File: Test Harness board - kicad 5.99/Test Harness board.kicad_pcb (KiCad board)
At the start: 4 copper layers, 233 x 70 mm, 133 parts, among them U1 TCA9548APWR

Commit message: restart with the test harness board
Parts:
- removed D_TEST1, D_TEST2: LED_Small, LED_SMD:LED_1206_3216Metric_Castellated
- UL1, UL3, UL4, UL5: footprint Package_SO:SSOP-28_5.3x10.2mm_P0.65mm -> Package_SO:TSSOP-28_4.4x9.7mm_P0.65mm
- UL1_1, UL1_2, UL2_1, UL2_2, UL3_1, UL3_2, UL4_1, UL4_2, UL5_1, UL5_2: footprint Package_SO:TSSOP-20_4.4x6.5mm_P0.65mm -> Package_SO:SOIC-20W_7.5x12.8mm_P1.27mm
- UL2: footprint Package_SO:SSOP-28_5.3x10.2mm_P0.65mm -> Package_SO:SOIC-28W_7.5x17.9mm_P1.27mm
- moved CL1_1 359.1 mm to (-151.7, 118.8), turned to 0 degrees
- moved CL3_2 334.8 mm to (-134.6, 102.0)
- moved CL4 325.0 mm to (-128.6, 95.4)
- moved UL3_1 316.4 mm to (-200.8, 111.7)
- moved D_A11 314.1 mm to (-217.1, 125.7), turned to 0 degrees
- moved CL4_1 310.9 mm to (-108.4, 76.0)
- moved CL1_2 310.9 mm to (-123.1, 90.7), turned to 0 degrees
- moved RNL3_1_2 307.7 mm to (-186.1, 109.6), turned to 0 degrees
- moved RNL1_1_2 305.8 mm to (-186.1, 102.8), turned to 0 degrees
- moved RNL1_2_2 298.9 mm to (-199.0, 122.3), turned to 0 degrees
- moved CL1 297.6 mm to (-96.3, 66.1)
- moved RNL3_2_2 291.3 mm to (-191.6, 102.8), turned to 0 degrees
- moved CL3 291.2 mm to (-95.5, 61.8)
- moved CL3_1 291.2 mm to (-84.0, 51.8)
- moved D_L11 289.8 mm to (-175.7, 124.5), turned to 0 degrees
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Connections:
- J_LEFT1 pad a11: Net-(J_LEFT1-Pada11) -> GND
- J_LEFT1 pad a15: Net-(J_LEFT1-Pada15) -> GND
- J_LEFT1 pad a17: Net-(J_LEFT1-Pada17) -> GND
- J_LEFT1 pad a19: Net-(J_LEFT1-Pada19) -> GND
- J_LEFT1 pad a32: Net-(J_LEFT1-Pada32) -> +5V
- J_LEFT1 pad a9: Net-(J_LEFT1-Pada9) -> GND
- J_LEFT1 pad b1: Net-(J_LEFT1-Padb1) -> +5V
- J_LEFT1 pad b11: Net-(J_LEFT1-Padb11) -> +5V
- J_LEFT1 pad b12: Net-(J_LEFT1-Padb12) -> GND
- J_LEFT1 pad b13: Net-(J_LEFT1-Padb13) -> +5V
- J_LEFT1 pad b17: Net-(J_LEFT1-Padb17) -> +5V
- J_LEFT1 pad b20: Net-(J_LEFT1-Padb20) -> GND
- J_LEFT1 pad b21: Net-(J_LEFT1-Padb21) -> +5V
- J_LEFT1 pad b22: Net-(J_LEFT1-Padb22) -> GND
- J_LEFT1 pad b23: Net-(J_LEFT1-Padb23) -> GND
- J_LEFT1 pad b24: Net-(J_LEFT1-Padb24) -> +5V
- J_LEFT1 pad b27: Net-(J_LEFT1-Padb27) -> +5V
- J_LEFT1 pad b31: Net-(J_LEFT1-Padb31) -> GND
- J_LEFT1 pad b32: Net-(J_LEFT1-Padb32) -> +5V
- J_LEFT1 pad c32: Net-(J_LEFT1-Padc32) -> +5V
- J_LEFT1 pad c9: Net-(J_LEFT1-Padc9) -> GND
- UL3 pad 1: /Left connector/A21 -> /Left connector/A13
- UL3 pad 2: /Left connector/A20 -> /Left connector/A12
- UL3 pad 21: /Left connector/A13 -> /Left connector/A21
- UL3 pad 22: /Left connector/A12 -> /Left connector/A20
- UL3 pad 23: /Left connector/A11 -> /Left connector/A19
- UL3 pad 24: /Left connector/A10 -> /Left connector/A18
- UL3 pad 25: /Left connector/A9 -> /Left connector/A17
- UL3 pad 26: /Left connector/A8 -> /Left connector/A16
- UL3 pad 27: /Left connector/A7 -> /Left connector/A15
- UL3 pad 28: /Left connector/A6 -> /Left connector/A14
- UL3 pad 3: /Left connector/A19 -> /Left connector/A11
- UL3 pad 4: /Left connector/A18 -> /Left connector/A10
- UL3 pad 5: /Left connector/A17 -> /Left connector/A9
- UL3 pad 6: /Left connector/A16 -> /Left connector/A8
- UL3 pad 7: /Left connector/A15 -> /Left connector/A7
- UL3 pad 8: /Left connector/A14 -> /Left connector/A6
- UL5 pad 1: /Left connector/MEMORY -> Net-(UL5-Pad1)
- UL5 pad 21: /Left connector/_PSEL1 -> /Left connector/IR1
- UL5 pad 22: /Left connector/_RD -> /Left connector/IR2
- UL5 pad 23: /Left connector/_WR -> /Left connector/IR3
- UL5 pad 24: /Left connector/XL_MDR_LO -> /Left connector/XL_MDR_HI
- UL5 pad 25: /Left connector/XL_MDR_HI -> /Left connector/XL_MDR_LO
- UL5 pad 26: /Left connector/IR3 -> /Left connector/_WR
- UL5 pad 27: /Left connector/IR2 -> /Left connector/_RD
- UL5 pad 28: /Left connector/IR1 -> /Left connector/_PSEL1
- UL5 pad 3: /Left connector/MEMREF -> Net-(UL5-Pad3)
- UL5 pad 4: /Left connector/_RESET -> /Left connector/_IRQ4
- UL5 pad 5: /Left connector/_STOP_CLK -> /Left connector/MEMREF
- UL5 pad 6: Net-(UL5-Pad6) -> /Left connector/MEMORY
- UL5 pad 7: Net-(UL5-Pad7) -> /Left connector/_RESET
- UL5 pad 8: /Left connector/_IRQ4 -> /Left connector/_STOP_CLK
- UL5_1 pad 11: /Left connector/_IRQ4 -> /Left connector/_STOP_CLK
- UL5_1 pad 12: /Left connector/D__RESET -> /Left connector/D__IRQ4
- UL5_1 pad 13: Net-(UL5_1-Pad13) -> /Left connector/_RESET
- UL5_1 pad 14: /Left connector/D_MEMREF -> Net-(UL5_1-Pad14)
- UL5_1 pad 15: Net-(UL5_1-Pad15) -> /Left connector/MEMORY
- UL5_1 pad 17: /Left connector/_STOP_CLK -> /Left connector/MEMREF
- UL5_1 pad 18: /Left connector/D_MEMORY -> Net-(UL5_1-Pad18)
- UL5_1 pad 2: /Left connector/MEMORY -> Net-(UL5_1-Pad2)
- UL5_1 pad 3: /Left connector/D__STOP_CLK -> /Left connector/D_MEMREF
- UL5_1 pad 5: Net-(UL5_1-Pad5) -> /Left connector/D_MEMORY
- UL5_1 pad 6: /Left connector/MEMREF -> Net-(UL5_1-Pad6)
- UL5_1 pad 7: Net-(UL5_1-Pad7) -> /Left connector/D__RESET
- UL5_1 pad 8: /Left connector/_RESET -> /Left connector/_IRQ4
- UL5_1 pad 9: /Left connector/D__IRQ4 -> /Left connector/D__STOP_CLK
- UL5_2 pad 14: /Left connector/D_WR -> /Left connector/D__WR
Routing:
- net /Left connector/MAR10: track 0.00 -> 67.2 mm
- net /Left connector/MAR11: track 0.00 -> 62.0 mm
- net /Left connector/MAR12: track 0.00 -> 61.6 mm
- net /Left connector/L15: track 0.00 -> 59.2 mm, vias 0 -> 3
- net /Left connector/L14: track 0.00 -> 57.5 mm, vias 0 -> 3
- net /Left connector/MAR13: track 0.00 -> 56.2 mm
- net /Left connector/MAR14: track 0.00 -> 51.1 mm
- net /Left connector/L13: track 0.00 -> 50.6 mm, vias 0 -> 3
- net /Left connector/L0: track 0.00 -> 50.1 mm, vias 0 -> 3
- net /Left connector/L1: track 0.00 -> 49.4 mm, vias 0 -> 3
- net /Left connector/L2: track 0.00 -> 45.2 mm, vias 0 -> 3
- net /Left connector/L12: track 0.00 -> 45.1 mm, vias 0 -> 3
- net /Left connector/L3: track 0.00 -> 43.5 mm, vias 0 -> 3
- net /Left connector/L11: track 0.00 -> 39.8 mm, vias 0 -> 3
- net /Left connector/L4: track 0.00 -> 38.6 mm, vias 0 -> 3
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- added copper zone on In1.Cu, net +5V
- added copper zone on In2.Cu, net GND
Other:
- board size 233 x 70 mm -> 233 x 160 mm

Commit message: oops, had the connector on the wrong side !
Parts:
- D_A0, D_A1, D_A10, D_A11, D_A12, D_A13, D_A14, D_A15, D_A16, D_A17, D_A18, D_A19, D_A2, D_A20, D_A21, D_A3, D_A4, D_A5, D_A6, D_A7, D_A8, D_A9, D_D0, D_D1, D_D2, D_D3, D_D4, D_D5, D_D6, D_D7, D_IR2, D_IR3, D_L0, D_L1, D_L10, D_L11, D_L12, D_L13, D_L14, D_L15, D_L2, D_L3, D_L4, D_L5, D_L6, D_L7, D_L8, D_L9, D_MAR0, D_MAR1, D_MAR10, D_MAR11, D_MAR12, D_MAR13, D_MAR14, D_MAR15, D_MAR2, D_MAR3, D_MAR4, D_MAR5, D_MAR6, D_MAR7, D_MAR8, D_MAR9, D_MEMORY1, D_MEMREF1, D_XL_MDR_HI1, D_XL_MDR_LO1, D__IR1, D__IRQ4, D__PSEL1, D__RD1, D__RESET1, D__STOP_CLK1, D__WR1: footprint LED_SMD:LED_1206_3216Metric_Castellated -> LED_SMD:LED_0805_2012Metric
- UL1_1, UL1_2, UL2_1, UL2_2, UL3_1, UL3_2, UL4_1, UL4_2, UL5_1, UL5_2: footprint Package_SO:SOIC-20W_7.5x12.8mm_P1.27mm -> Package_SO:TSSOP-20_4.4x6.5mm_P0.65mm
- UL2: footprint Package_SO:SOIC-28W_7.5x17.9mm_P1.27mm -> Package_SO:TSSOP-28_4.4x9.7mm_P0.65mm
- moved UL4_1 224.4 mm to (46.8, 126.4)
- moved D_MAR7 171.9 mm to (30.9, 92.1), turned to 90 degrees
- moved D_L3 162.9 mm to (27.9, 92.0), turned to 90 degrees
- moved D_MAR8 160.3 mm to (19.9, 92.0), turned to -90 degrees
- moved D_D0 157.8 mm to (22.9, 92.0), turned to 90 degrees
- moved UL4_2 154.9 mm to (33.5, 127.3)
- moved D__PSEL1 151.4 mm to (16.9, 92.0), turned to 90 degrees
- moved D_A12 148.3 mm to (13.9, 92.0), turned to 90 degrees
- moved J_LEFT1 133.0 mm to (175.6, 30.3)
- moved UL5 131.1 mm to (220.8, 59.8)
- moved UL3 130.6 mm to (206.6, 59.8)
- moved UL1 128.6 mm to (190.9, 59.8)
- moved UL4 126.6 mm to (175.1, 59.8)
- moved UL2 123.3 mm to (236.6, 59.8)
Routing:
- net /Left connector/_PSEL1: track 0.00 -> 68.0 mm, vias 0 -> 3
- net /Left connector/MEMORY: track 7.42 -> 73.1 mm, vias 0 -> 3
- net /Left connector/MAR15: track 6.71 -> 69.3 mm, vias 0 -> 3
- net /Left connector/MAR9: track 0.00 -> 60.3 mm, vias 0 -> 2
- net /Left connector/MAR8: track 0.00 -> 58.8 mm, vias 0 -> 2
- net /Left connector/IR3: track 0.00 -> 53.8 mm, vias 0 -> 3
- net /Left connector/_IRQ4: track 0.00 -> 53.0 mm, vias 0 -> 3
- net /Left connector/IR2: track 0.00 -> 51.5 mm, vias 0 -> 3
- net /Left connector/MEMREF: track 0.00 -> 49.2 mm, vias 0 -> 3
- net /Left connector/IR1: track 0.00 -> 49.0 mm, vias 0 -> 3
- net /Left connector/A21: track 0.00 -> 48.5 mm, vias 0 -> 2
- net /Left connector/A20: track 0.00 -> 45.7 mm, vias 0 -> 2
- net /Left connector/A19: track 0.00 -> 43.2 mm, vias 0 -> 2
- net /Left connector/MAR0: track 0.00 -> 43.0 mm, vias 0 -> 2
- net /Left connector/_WR: track 0.00 -> 42.2 mm, vias 0 -> 3
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
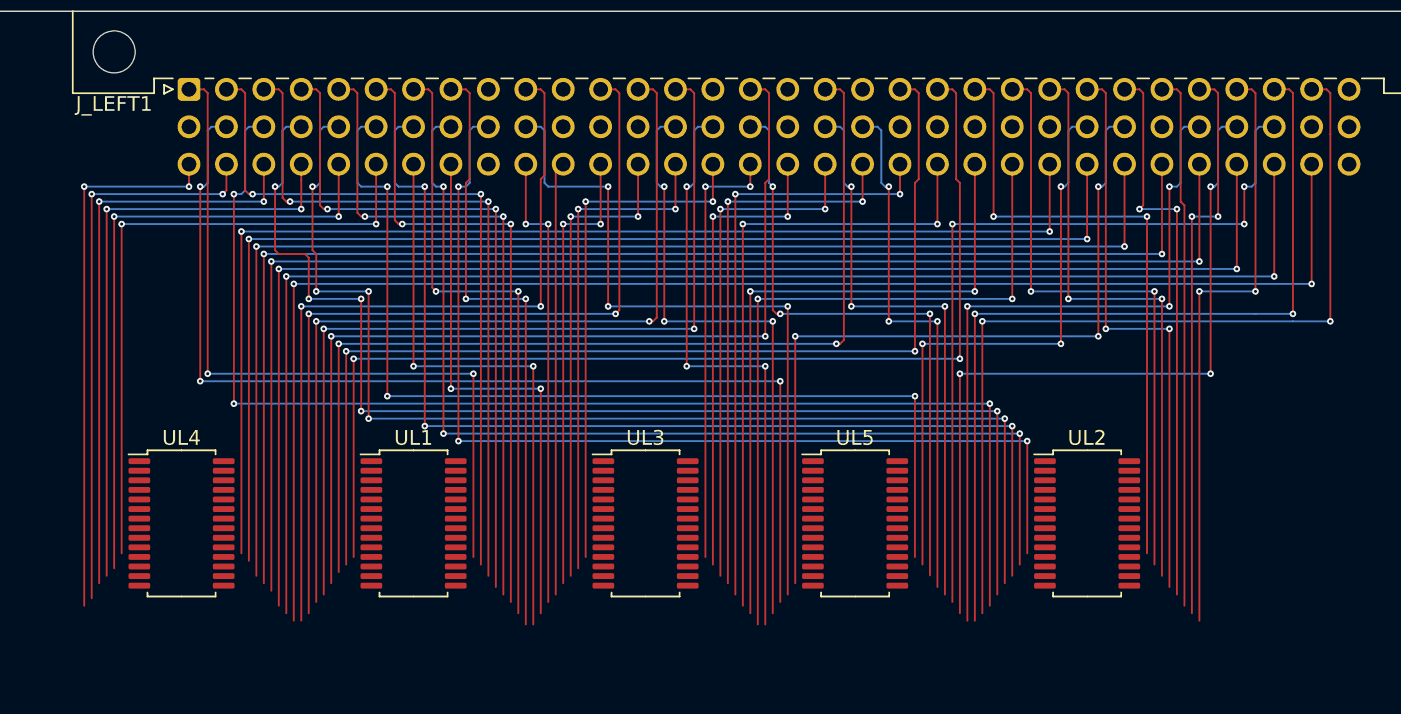
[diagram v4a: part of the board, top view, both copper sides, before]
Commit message: fix via to via distance according to the rules, hope that works
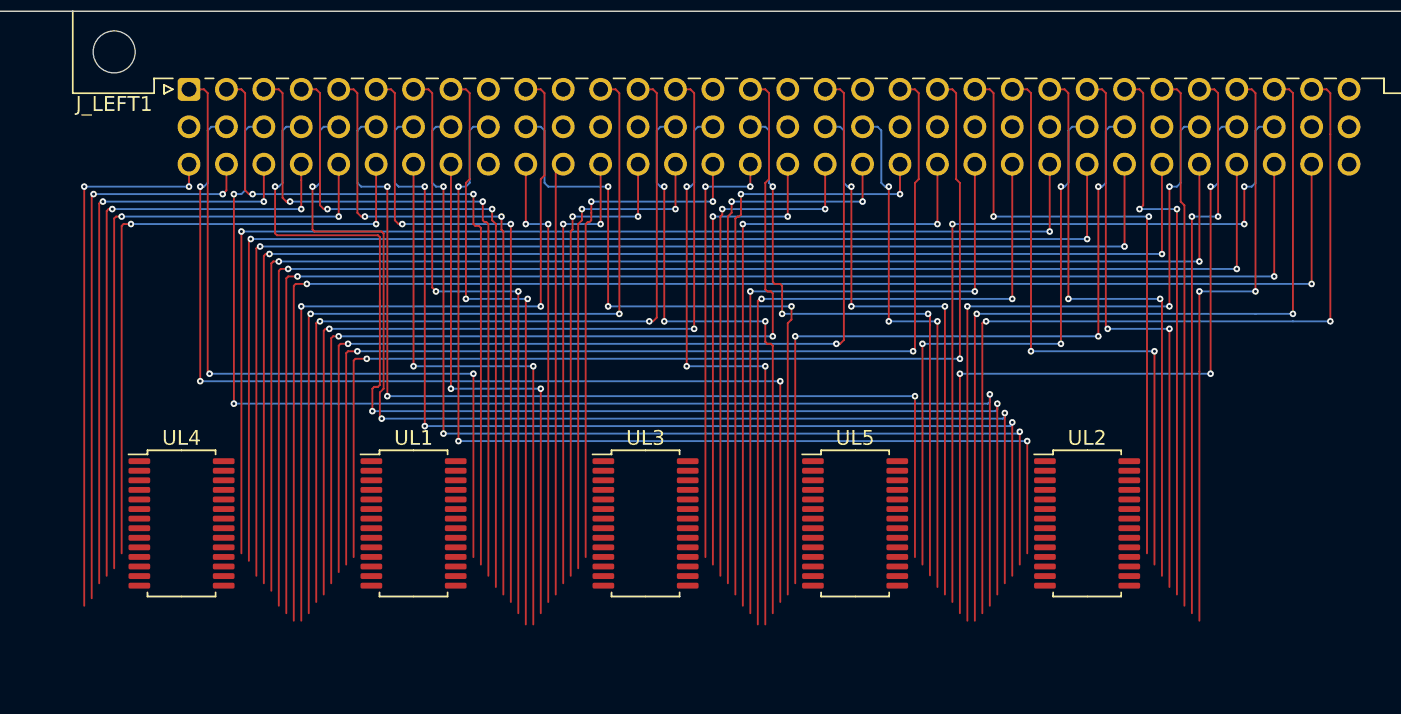
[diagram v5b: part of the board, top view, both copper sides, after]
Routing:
- net /Left connector/MAR11: track 82.0 -> 84.2 mm, vias 5 -> 3
- net /Left connector/MAR10: track 85.6 -> 86.8 mm
- net /Left connector/MAR12: track 79.3 -> 80.3 mm, vias 5 -> 3
- net /Left connector/L12: track 64.2 -> 65.0 mm

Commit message: muck around with component placement
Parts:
- moved UL2_2 452.1 mm to (251.2, 87.1)
- moved UL5_1 436.7 mm to (221.3, 77.3)
- moved UL2_1 428.6 mm to (240.8, 77.3)
- moved UL5_2 418.9 mm to (231.0, 87.1)
- moved UL3_1 412.4 mm to (210.9, 87.1)
- moved UL3_2 376.1 mm to (201.1, 77.3)
- moved UL1_2 352.9 mm to (190.7, 87.1)
- moved UL1_1 343.5 mm to (181.0, 77.3)
- moved A1 233.9 mm to (141.0, 143.0)
- moved J_PWR1 218.2 mm to (125.0, 180.0)
- moved UL4_2 143.5 mm to (171.2, 87.1)
- moved UL4_1 124.1 mm to (160.8, 77.3)
- moved U1 27.7 mm to (-41.0, 80.2)
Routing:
- net /Left connector/A5: track 43.6 -> 39.7 mm, vias 2 -> 3
- net /Left connector/A3: track 41.1 -> 37.3 mm, vias 2 -> 3
- net /Left connector/A4: track 42.6 -> 38.9 mm, vias 2 -> 3
- net /Left connector/D0: track 81.3 -> 77.9 mm, vias 2 -> 3
- net /Left connector/D1: track 83.7 -> 80.5 mm, vias 2 -> 3
- net /Left connector/A1: track 38.4 -> 35.6 mm, vias 2 -> 3
- net /Left connector/D2: track 86.8 -> 84.1 mm, vias 2 -> 3
- net /Left connector/A2: track 39.5 -> 37.0 mm, vias 2 -> 3
- net /Left connector/D3: track 89.3 -> 86.8 mm, vias 2 -> 3
- net /Left connector/D5: track 94.9 -> 93.2 mm, vias 2 -> 3
- net /Left connector/A0: track 37.1 -> 35.6 mm, vias 2 -> 3
- net /Left connector/D4: track 91.9 -> 90.5 mm, vias 2 -> 3
- net /Left connector/D6: track 97.5 -> 96.9 mm, vias 2 -> 3
- net /Left connector/D7: track 100.0 -> 99.6 mm, vias 2 -> 3

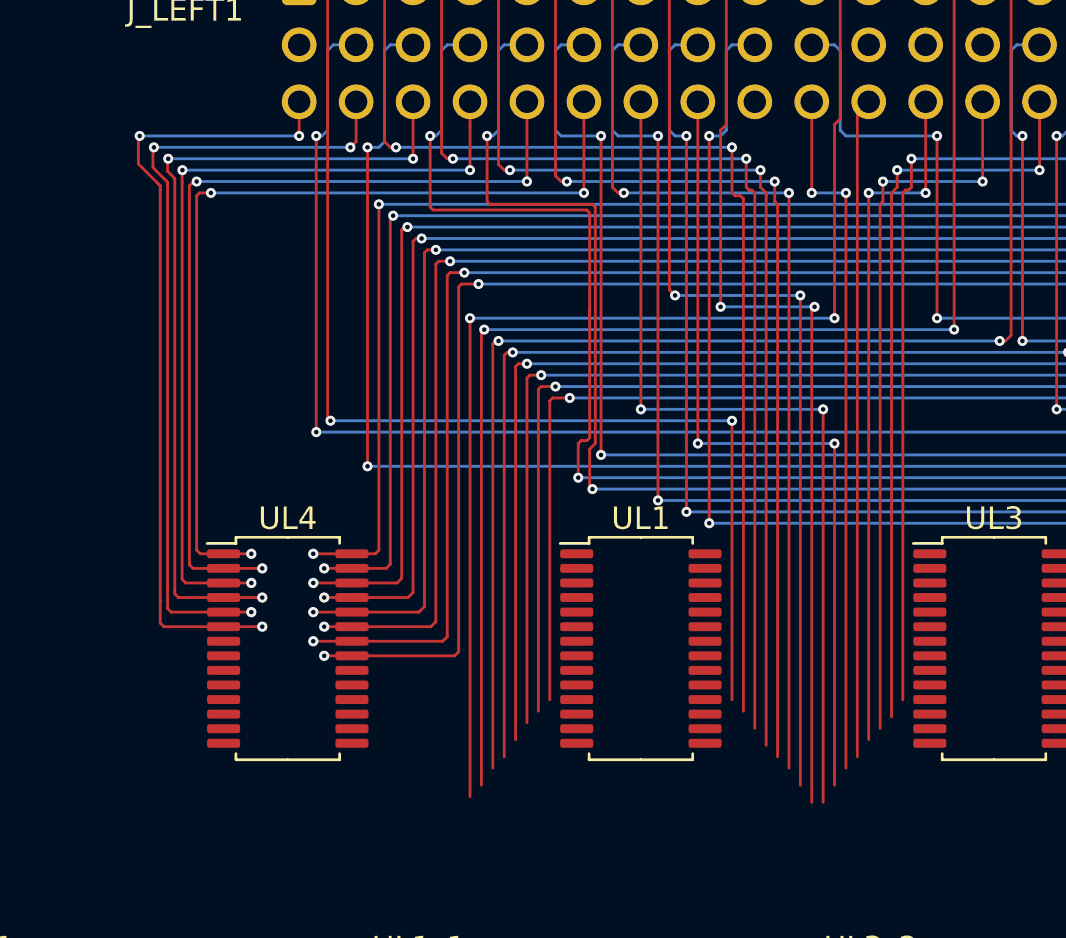
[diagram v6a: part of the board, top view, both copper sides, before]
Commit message: move ALU board to a versionned directory
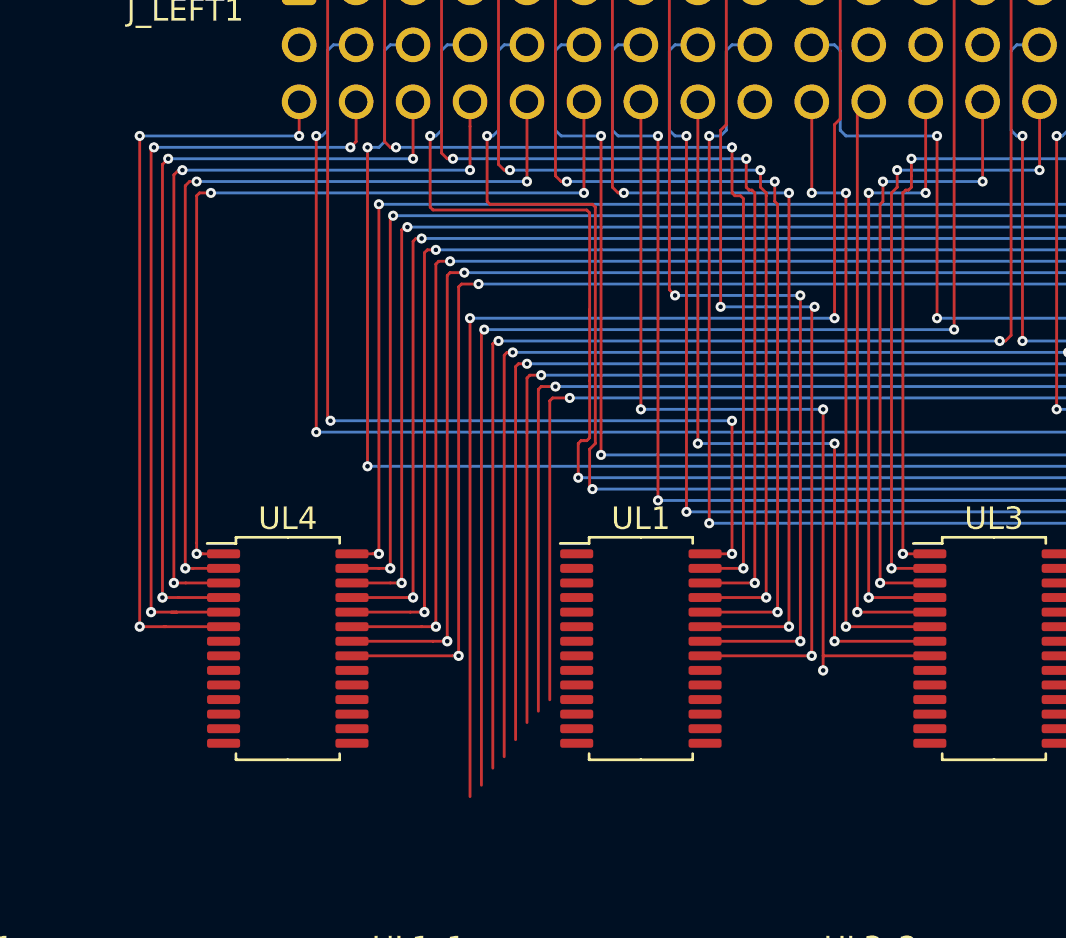
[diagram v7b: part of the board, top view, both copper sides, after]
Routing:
- net /Left connector/A13: track 35.2 -> 29.8 mm, vias 2 -> 3
- net /Left connector/L0: track 50.8 -> 45.5 mm, vias 2 -> 3
- net /Left connector/A12: track 33.9 -> 29.0 mm, vias 2 -> 3
- net /Left connector/L1: track 49.1 -> 44.4 mm, vias 2 -> 3
- net /Left connector/L2: track 47.8 -> 43.6 mm, vias 2 -> 3
- net /Left connector/A11: track 32.4 -> 28.2 mm, vias 2 -> 3
- net /Left connector/L3: track 46.5 -> 42.7 mm, vias 2 -> 3
- net /Left connector/A10: track 31.0 -> 27.4 mm, vias 2 -> 3
- net /Left connector/A9: track 29.4 -> 26.2 mm, vias 0 -> 1
- net /Left connector/L4: track 45.1 -> 41.9 mm, vias 2 -> 3
- net /Left connector/L5: track 43.6 -> 41.1 mm, vias 2 -> 3
- net /Left connector/A8: track 31.2 -> 28.7 mm, vias 2 -> 3
- net /Left connector/L6: track 42.4 -> 40.2 mm, vias 2 -> 3
- net /Left connector/A7: track 36.6 -> 34.4 mm, vias 2 -> 3
- net /Left connector/L7: track 41.8 -> 40.0 mm, vias 2 -> 3
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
